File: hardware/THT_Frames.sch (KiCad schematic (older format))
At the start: 144 parts, among them J1 FRAME_IN, J10 1_OUT, J11 2_OUT, J12 3_OUT, J13 4_OUT, J14 POWER, J15 OFFSET_JUMPER, J16 ALL_IN, J17 MIX_OUT, J18 Conn_01x12_Male, J19 Conn_01x12_Female, J2 Serial, J20 Conn_01x12_Female, J21 Conn_01x12_Male, J22 Conn_01x12_Female, J3 Conn_01x12_Male, J5 STEP_OUT, J6 1_IN, J7 2_IN, J8 3_IN, J9 4_IN, Q1 2N3904, SW1 ADD, SW2 DEL, SW3 OFFSET, U1 TL072, U12 V2164, U13 TL072, U2 bluepill, U3 LM1117-3.3, U4 LM4040AIZ-10, U5 TL072, U6 MCP4822, U7 MCP4822, U8 TL074, U9 TL074

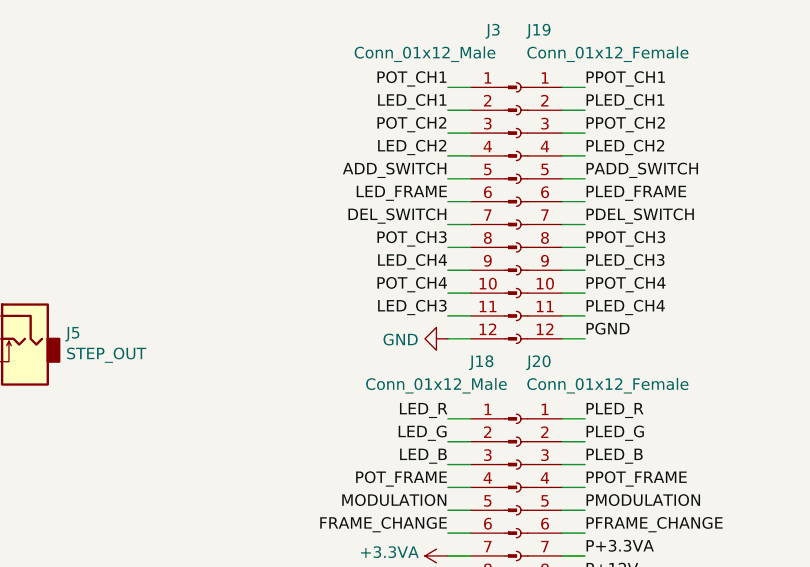
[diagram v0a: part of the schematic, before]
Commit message: Fix swapped leds on channels 3/4
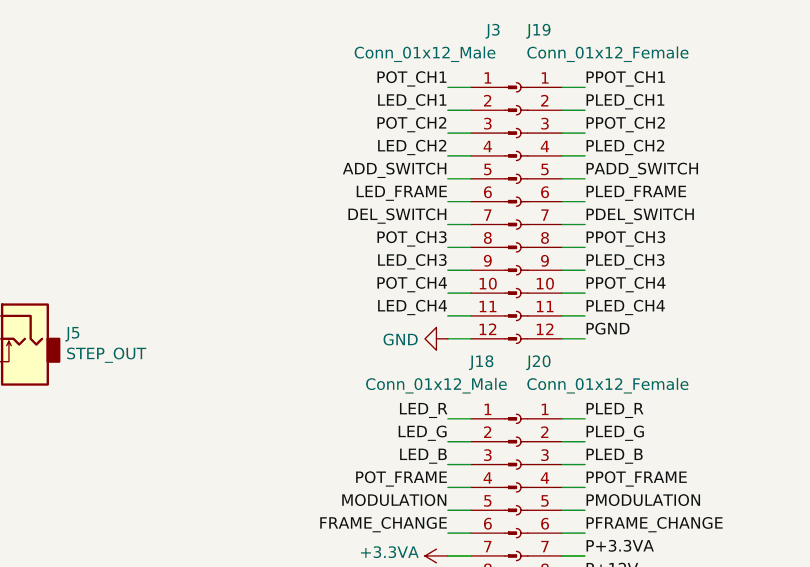
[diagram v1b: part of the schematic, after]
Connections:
- net LED_CH3: now also J3.9 (Pin_9); no longer J3.11 (Pin_11)
- net LED_CH4: now also J3.11 (Pin_11); no longer J3.9 (Pin_9)
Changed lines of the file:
@@
 Text Label 11500 9250 2    50   ~ 0
 LED_CH2
+Text Label 11500 9750 2    50   ~ 0
+LED_CH3
 Text Label 11500 9950 2    50   ~ 0
-LED_CH3
-Text Label 11500 9750 2    50   ~ 0
 LED_CH4
 Text Label 11500 9450 2    50   ~ 0

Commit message: Use easy to solder to-92 footprint, bigger footprints for 1uF caps
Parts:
- C24, C25, C28, C29: footprint custom:C_Disc_D5.0mm_W2.5mm_P5.00mm_silk -> custom:C_Disc_D7.5mm_W5.0mm_P5.00mm_silk
- Q1, U4: footprint custom:TO-92_Inline_silk -> custom:TO-92_Inline_Wide_silk
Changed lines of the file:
@@
 F 0 "Q1" H 8590 10396 50  0000 L CNN
 F 1 "2N3904" H 8590 10305 50  0000 L CNN
-F 2 "custom:TO-92_Inline_silk" H 8600 10275 50  0001 L CIN
+F 2 "custom:TO-92_Inline_Wide_silk" H 8600 10275 50  0001 L CIN
 F 3 "https://www.fairchildsemi.com/datasheets/2N/2N3904.pdf" H 8400 10350 50  0001 L CNN
 	1    8400 10350
@@
 F 0 "C24" H 11718 2196 50  0000 L CNN
 F 1 "1uF" H 11718 2105 50  0000 L CNN
-F 2 "custom:C_Disc_D5.0mm_W2.5mm_P5.00mm_silk" H 11638 2000 50  0001 C CNN
+F 2 "custom:C_Disc_D7.5mm_W5.0mm_P5.00mm_silk" H 11638 2000 50  0001 C CNN
 F 3 "~" H 11600 2150 50  0001 C CNN
 	1    11600 2150
@@
 F 0 "C28" H 12118 2196 50  0000 L CNN
 F 1 "1uF" H 12118 2105 50  0000 L CNN
-F 2 "custom:C_Disc_D5.0mm_W2.5mm_P5.00mm_silk" H 12038 2000 50  0001 C CNN
+F 2 "custom:C_Disc_D7.5mm_W5.0mm_P5.00mm_silk" H 12038 2000 50  0001 C CNN
 F 3 "~" H 12000 2150 50  0001 C CNN
 	1    12000 2150
@@
 F 0 "C25" H 11718 4196 50  0000 L CNN
 F 1 "1uF" H 11718 4105 50  0000 L CNN
-F 2 "custom:C_Disc_D5.0mm_W2.5mm_P5.00mm_silk" H 11638 4000 50  0001 C CNN
+F 2 "custom:C_Disc_D7.5mm_W5.0mm_P5.00mm_silk" H 11638 4000 50  0001 C CNN
 F 3 "~" H 11600 4150 50  0001 C CNN
 	1    11600 4150
@@
 F 0 "C29" H 12118 4196 50  0000 L CNN
 F 1 "1uF" H 12118 4105 50  0000 L CNN
-F 2 "custom:C_Disc_D5.0mm_W2.5mm_P5.00mm_silk" H 12038 4000 50  0001 C CNN
+F 2 "custom:C_Disc_D7.5mm_W5.0mm_P5.00mm_silk" H 12038 4000 50  0001 C CNN
 F 3 "~" H 12000 4150 50  0001 C CNN
 	1    12000 4150
@@
 F 0 "U4" V 5796 14312 50  0000 R CNN
 F 1 "LM4040AIZ-10" V 5705 14312 50  0000 R CNN
-F 2 "custom:TO-92_Inline_silk" H 5750 14200 50  0001 C CIN
+F 2 "custom:TO-92_Inline_Wide_silk" H 5750 14200 50  0001 C CIN
 F 3 "http://www.ti.com/lit/ds/symlink/lm4040-n.pdf" H 5750 14400 50  0001 C CIN
 	1    5750 14400

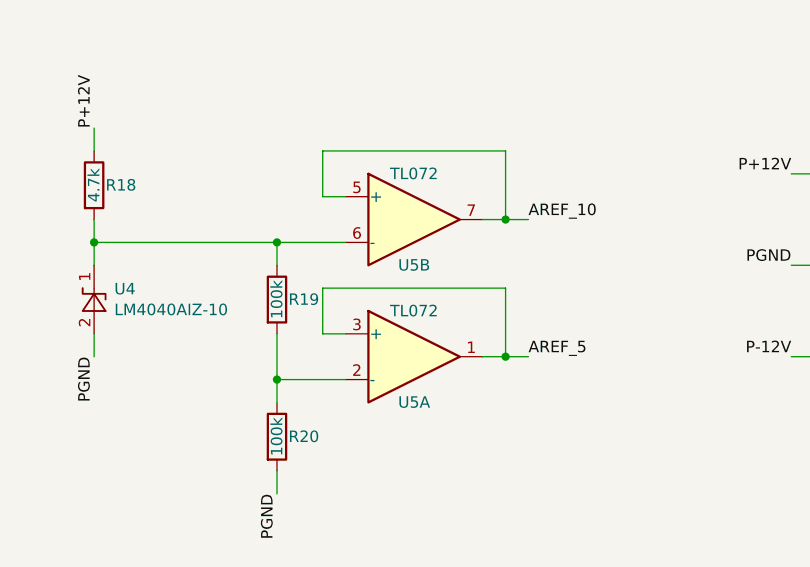
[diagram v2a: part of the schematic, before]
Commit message: Fix accidentally inverted internal offset voltages
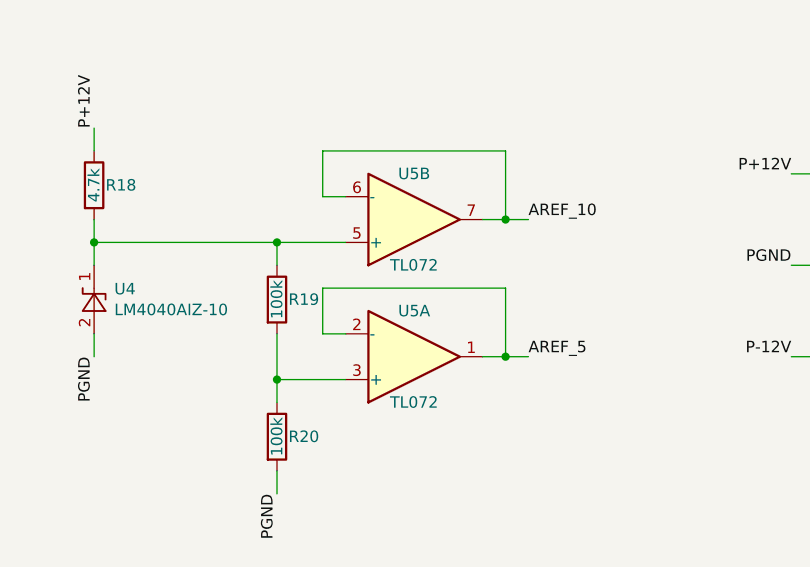
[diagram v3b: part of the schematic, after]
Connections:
- net AREF_10: now also U5.6 (-); no longer U5.5 (+)
- net AREF_5: now also U5.2 (-); no longer U5.3 (+)
- net at R18.2, R19.1, U4.1 (K): now also U5.5 (+); no longer U5.6 (-)
- net at R19.2, R20.1: now also U5.3 (+); no longer U5.2 (-)
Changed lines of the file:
@@
 F 3 "http://www.ti.com/lit/ds/symlink/tl071.pdf" H 7150 14650 50  0001 C CNN
 	1    7150 14650
-	1    0    0    -1
+	1    0    0    1
 $EndComp
 $Comp
@@
 F 3 "http://www.ti.com/lit/ds/symlink/tl071.pdf" H 7150 14050 50  0001 C CNN
 	2    7150 14050
-	1    0    0    -1
+	1    0    0    1
 $EndComp
 Text Label 7650 14650 0    50   ~ 0
